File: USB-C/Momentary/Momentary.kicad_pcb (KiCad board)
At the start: 4 copper layers, 32 x 84 mm, 40 parts, among them J1 Conn_02x04_Odd_Even, J2 USB_C_Receptacle_PowerOnly_6P, J3 Conn_02x04_Odd_Even, J4 AudioJack2_Ground, J5 AudioJack2_Ground, SW1 SW_Push, U1 LM27762, U2 74HC74, U3 OPA1655, U4 TMUX4053

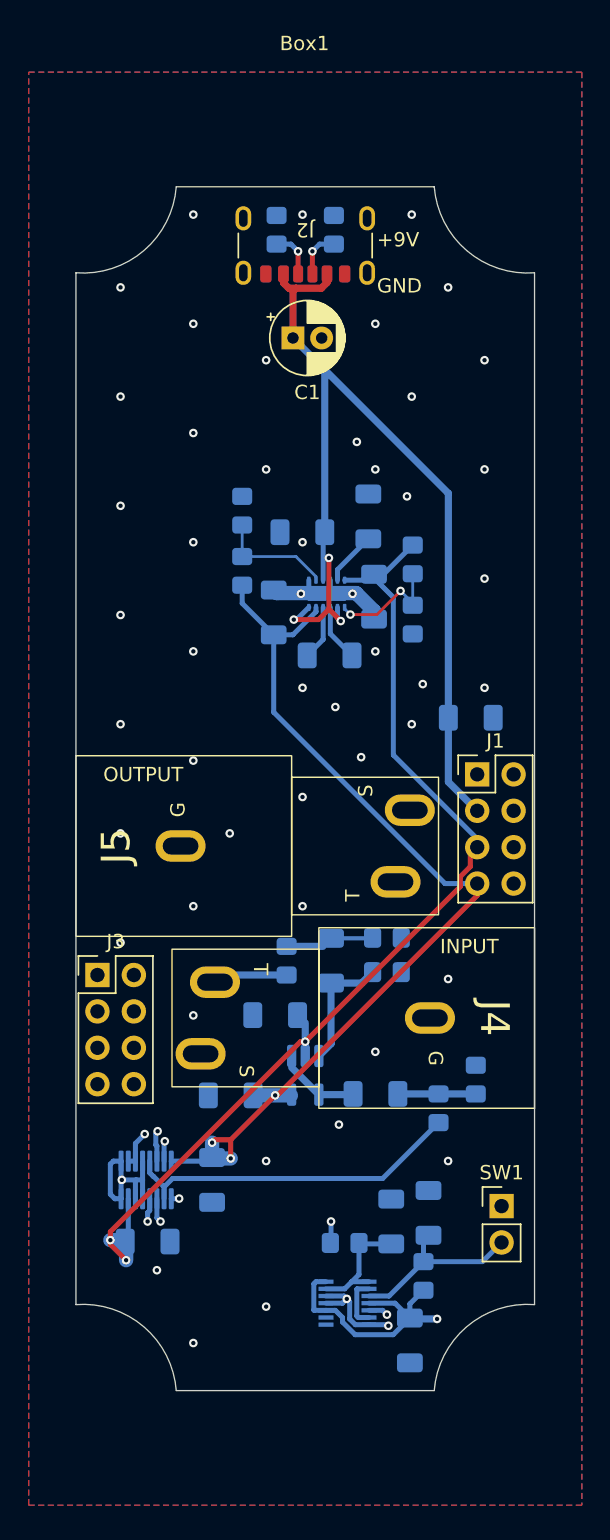
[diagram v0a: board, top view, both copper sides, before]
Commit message: Allow trimming gain on base board input buffer
Instead of just having a unity gain buffer, let's add a trim pot that
allows for higher input gain when that makes sense for the effect board.

For example, the very traditional Big Muff fuzz pedal seems to have an
input stage with roughly a voltage gain of 7x (+17dB).

Random pick: 100k trim pot with 10k resistor gives a gain range of 1-11.

Signed-off-by: Linus Torvalds <torvalds@linux-foundation.org>
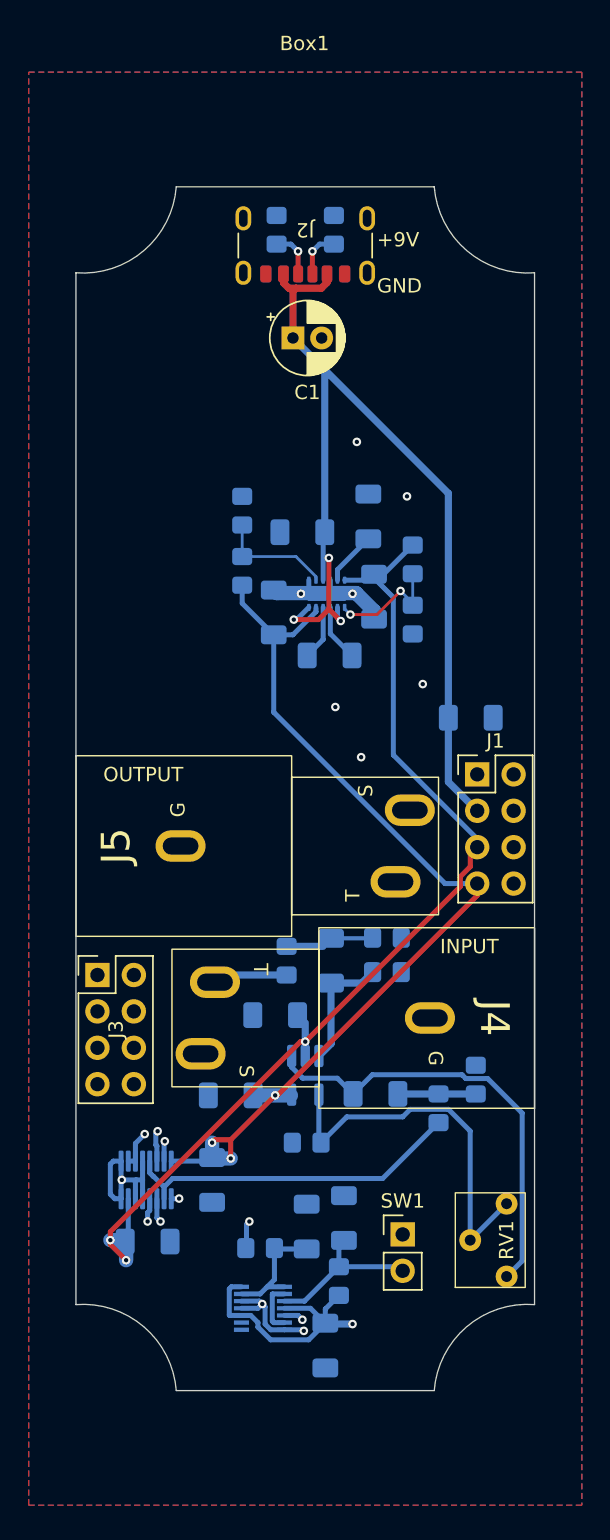
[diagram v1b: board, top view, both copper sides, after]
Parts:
- added R14: 10k, Resistor_SMD:R_0805_2012Metric_Pad1.20x1.40mm_HandSolder, B.Cu at (100.1, 124.7)
- added RV1: 100k, Mylib:Bourns_3362S, F.Cu at (114.0, 131.5)
- moved SW1 7.18 mm to (106.8, 131.1)
- moved C13 5.91 mm to (100.1, 130.6)
- moved R9 5.91 mm to (96.8, 132.1)
- moved R7 5.91 mm to (102.3, 134.4)
- moved U2 5.91 mm to (97.0, 136.3)
- moved C12 5.91 mm to (102.7, 130.0)
- moved C8 5.91 mm to (101.4, 138.9)
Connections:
- C11 pad 1: Net-(U3--) -> Net-(C11-Pad1)
- U3 pad 1: Net-(U3--) -> Net-(C11-Pad1)
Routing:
- net Net-(C11-Pad1): track 0.00 -> 31.2 mm
- net Net-(U3--): track 5.82 -> 26.6 mm
- net EFF^{ENA}: track 26.2 -> 21.5 mm
- net VIN: track 152.3 -> 156.3 mm
- net Net-(U2A-C): track 12.8 -> 10.8 mm
- net -V: track 74.3 -> 73.8 mm
- net GND: vias 52 -> 10
